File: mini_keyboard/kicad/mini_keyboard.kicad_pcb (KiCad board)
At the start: 2 copper layers, 158.8 x 114.3 mm, 86 parts, among them U1 MX1A-11NN, U10 MX1A-11NN, U100 DEV-15583, U101 ABX00027, U11 MX1A-11NN, U12 MX1A-11NN, U13 MX1A-11NN, U14 MX1A-11NN, U15 MX1A-11NN, U16 MX1A-11NN, U17 MX1A-11NN, U18 MX1A-11NN, U19 MX1A-11NN, U2 MX1A-11NN, U20 MX1A-11NN, U21 MX1A-11NN, U22 MX1A-11NN, U23 MX1A-11NN, U24 MX1A-11NN, U25 MX1A-11NN, U26 MX1A-11NN, U27 MX1A-11NN, U28 MX1A-11NN, U29 MX1A-11NN, U3 MX1A-11NN, U30 MX1A-11NN, U31 MX1A-11NN, U32 MX1A-11NN, U33 MX1A-11NN, U34 MX1A-11NN, U35 MX1A-11NN, U36 MX1A-11NN, U37 MX1A-11NN, U38 MX1A-11NN, U39 MX1A-11NN, U4 MX1A-11NN, U40 MX1A-11NN, U41 MX1A-11NN, U42 MX1A-11NN, U5 MX1A-11NN, U6 MX1A-11NN, U7 MX1A-11NN, U8 MX1A-11NN, U9 MX1A-11NN

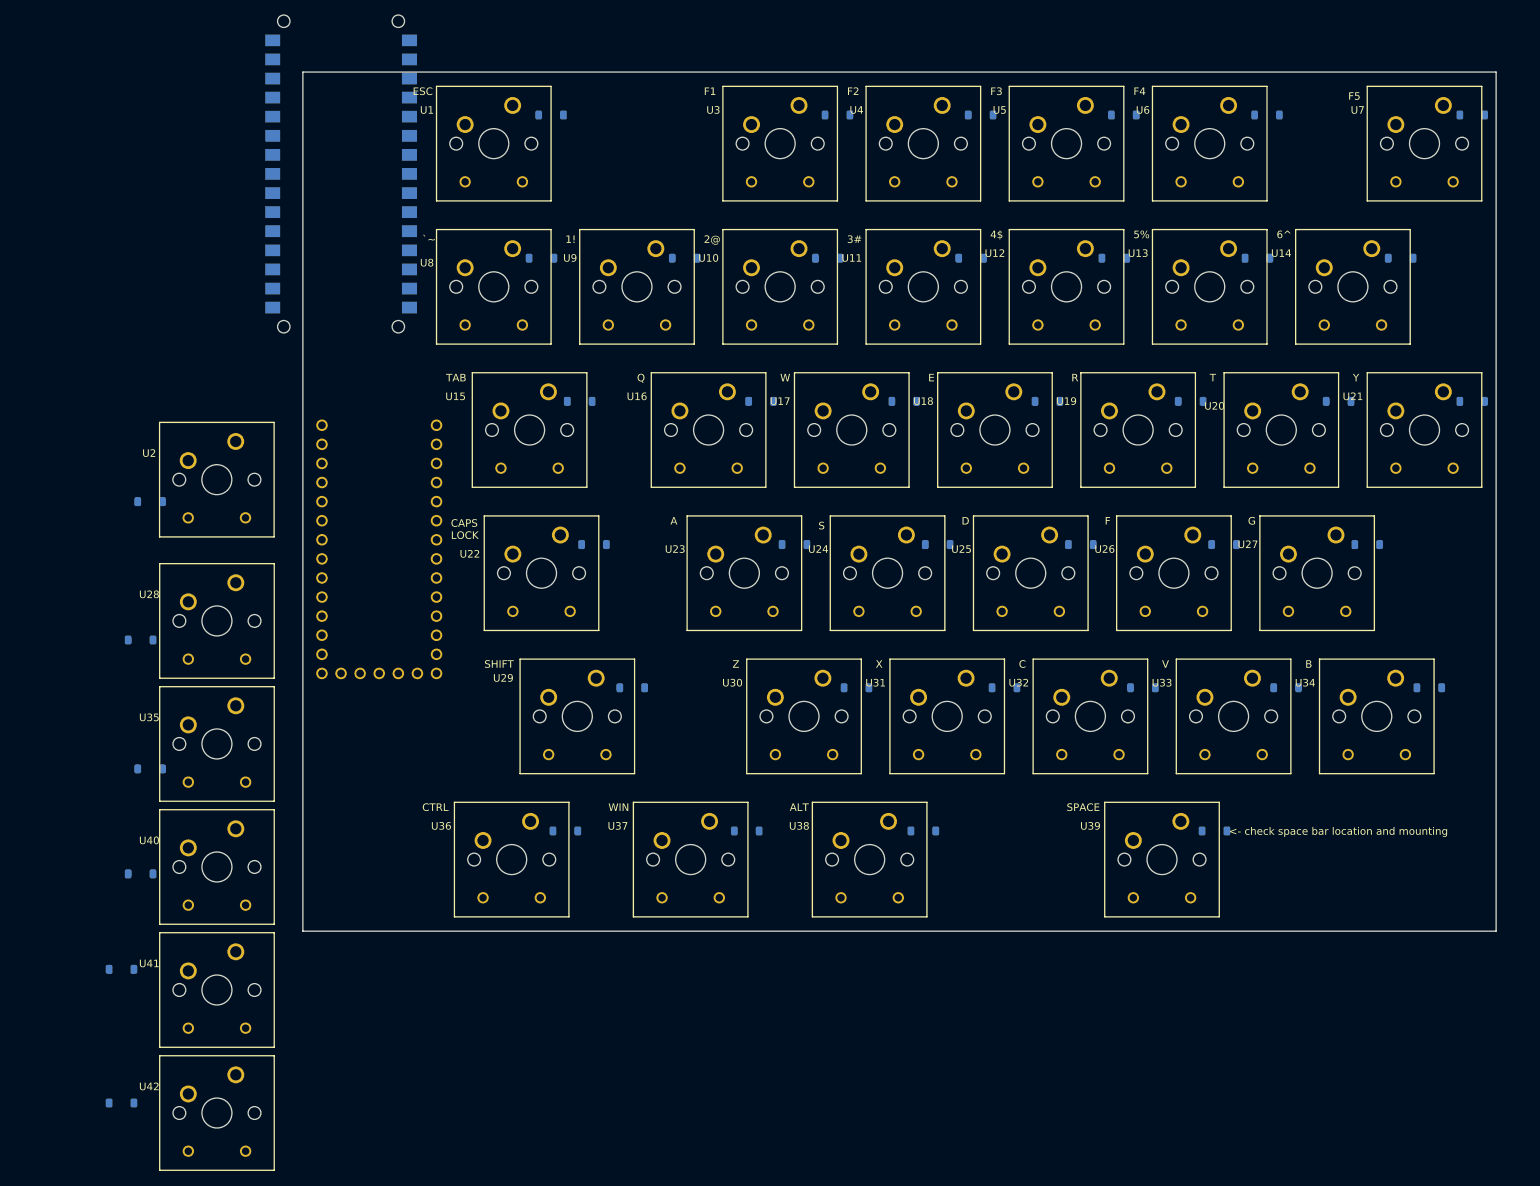
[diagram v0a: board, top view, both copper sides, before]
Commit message: rotated key switches 180 degreees
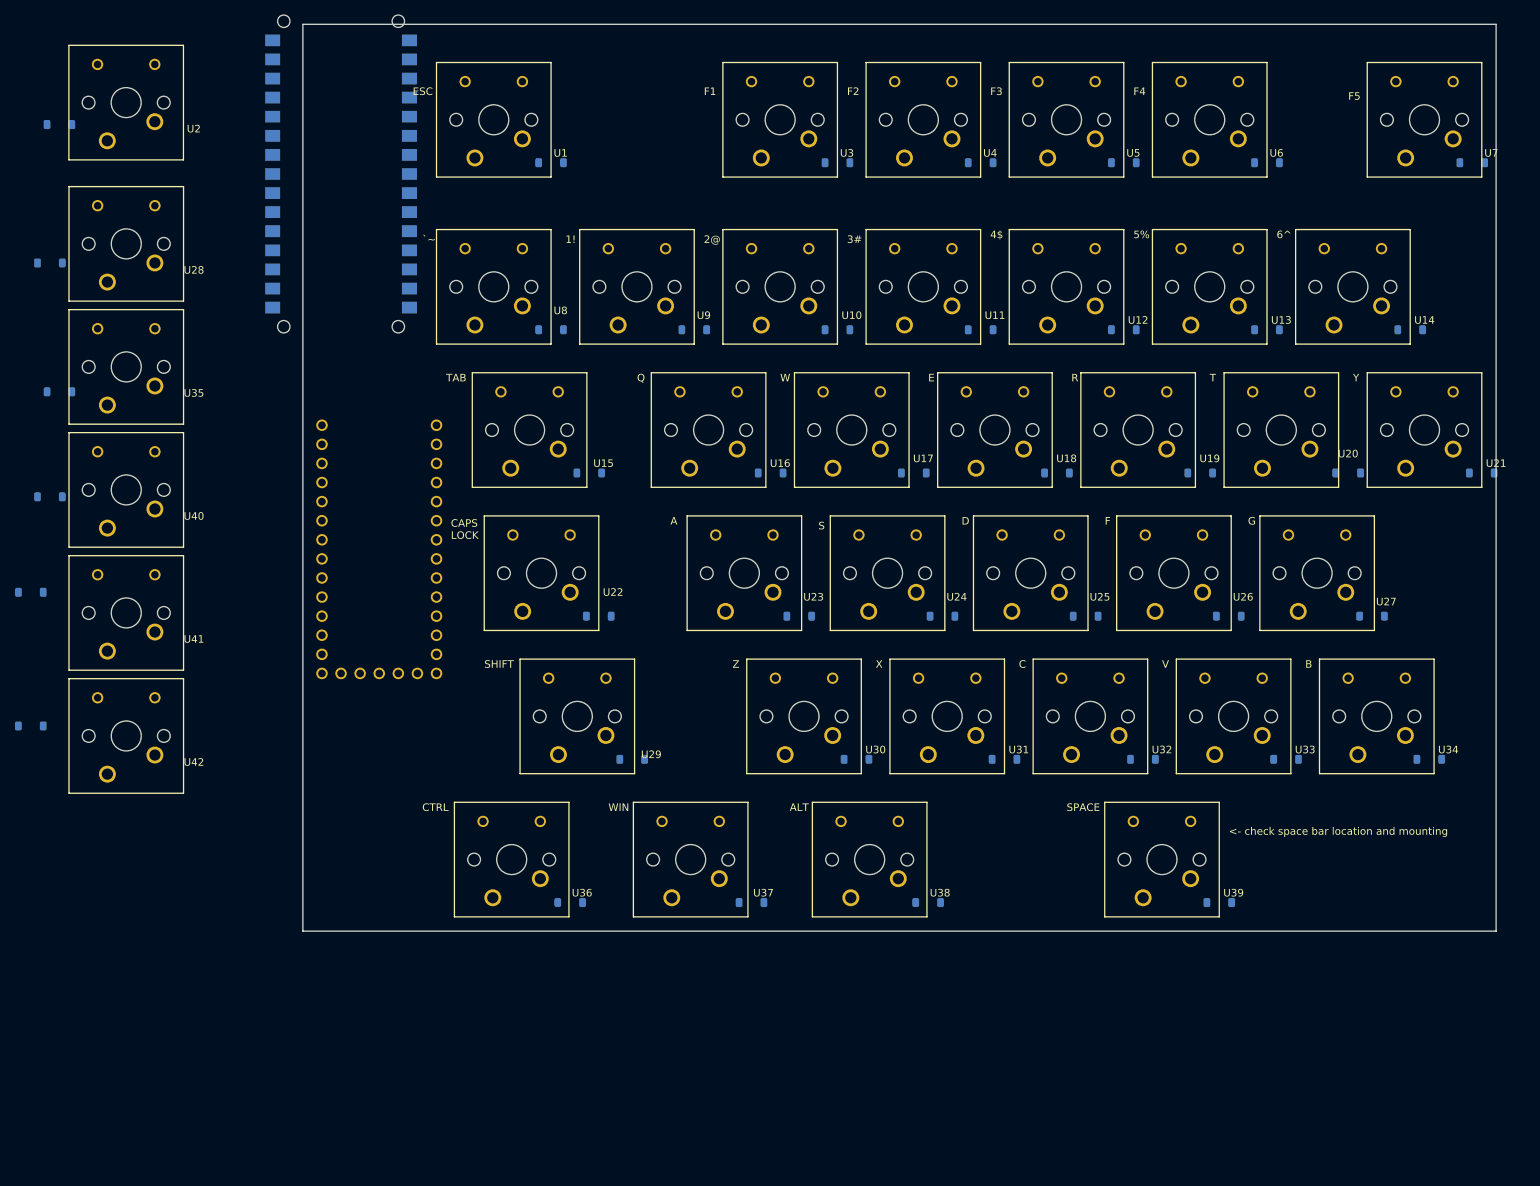
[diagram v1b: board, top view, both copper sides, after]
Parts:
- moved D28 51.6 mm to (-8.26, 50.8)
- moved D35 51.6 mm to (-6.99, 67.9)
- moved D40 51.6 mm to (-8.26, 81.9)
- moved D41 51.6 mm to (-10.8, 94.6)
- moved D42 51.6 mm to (-10.8, 112.4)
- moved U2 51.6 mm to (1.89, 29.5), turned to 180 degrees
- moved U35 51.6 mm to (1.91, 64.6), turned to 180 degrees
- moved U41 51.6 mm to (1.91, 97.4), turned to 180 degrees
- moved U42 51.6 mm to (1.91, 113.7), turned to 180 degrees
- moved D2 51.6 mm to (-6.99, 32.4)
- moved U28 51.6 mm to (1.91, 48.3), turned to 180 degrees
- moved U40 51.6 mm to (1.91, 81.0), turned to 180 degrees
- moved D12 9.61 mm to (134.6, 59.7)
- moved D14 9.61 mm to (172.7, 59.7)
- moved D8 9.61 mm to (58.4, 59.7)
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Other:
- board size 158.8 x 114.3 mm -> 158.8 x 120.6 mm

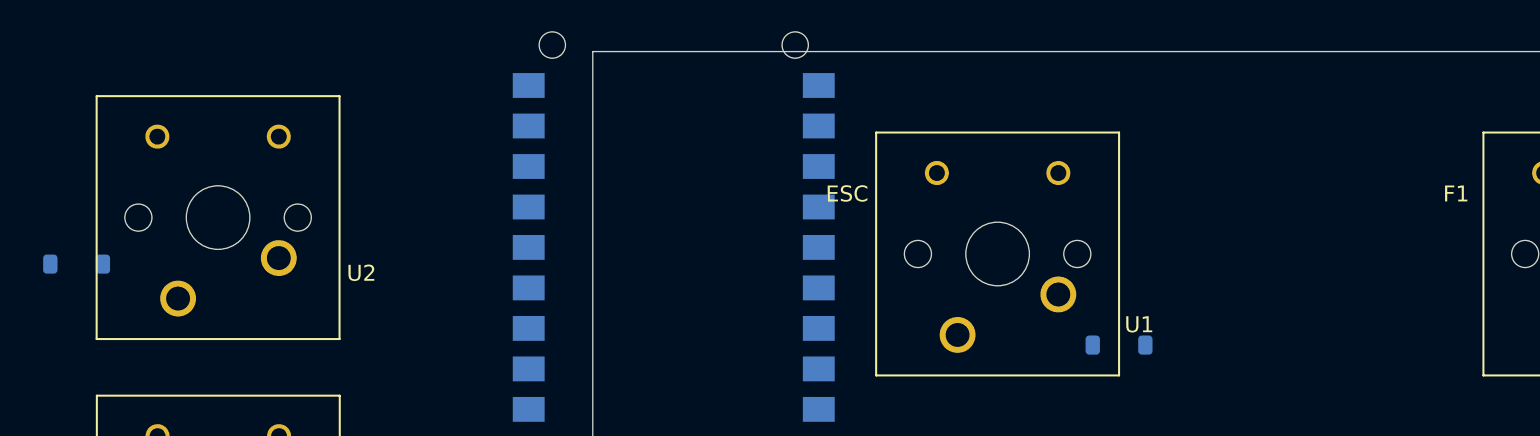
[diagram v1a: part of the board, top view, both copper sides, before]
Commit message: looking at PG151101S11 socket for MX switches.
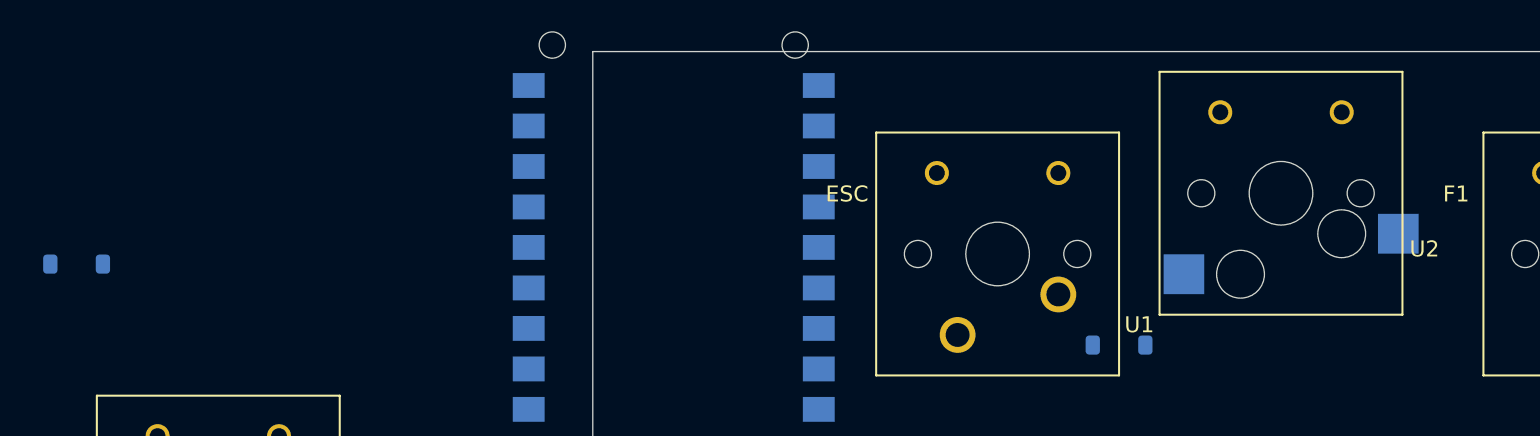
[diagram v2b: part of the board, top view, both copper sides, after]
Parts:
- added S1: PG151101S11, pedrolib:SW_PG151101S11, B.Cu at (69.2, 31.8)
- moved U2 66.7 mm to (68.6, 27.9)
